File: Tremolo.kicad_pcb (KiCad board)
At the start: 2 copper layers, 177.9 x 90.1 mm, 116 parts, among them J1 Input, J10 R1, J11 R2, J12 TRG, J13 GND, J1A1 LeftA, J1B1 LeftB, J1C1 LeftC, J2 GND, J2A1 SwitchA, J2B1 SwitchB, J2C1 SwitchC, J3 +9v, J3A1 RightA, J3B1 RightB, J3C1 RightC, J4 GND, J5 RateSlv, J6 Gnd, J7 L2, J8 L1, J9 RateTip, Q1 BC549C, Q2 BC549C, Q3 BC549C, Q4 J113, Q5 BC549C, Q6 BC549C, T1 LeftTr, T2 RightTr, U1 TL072, U2 TL072, U3 TL072, U4 TL074, U5 VACTL, U6 VACTR

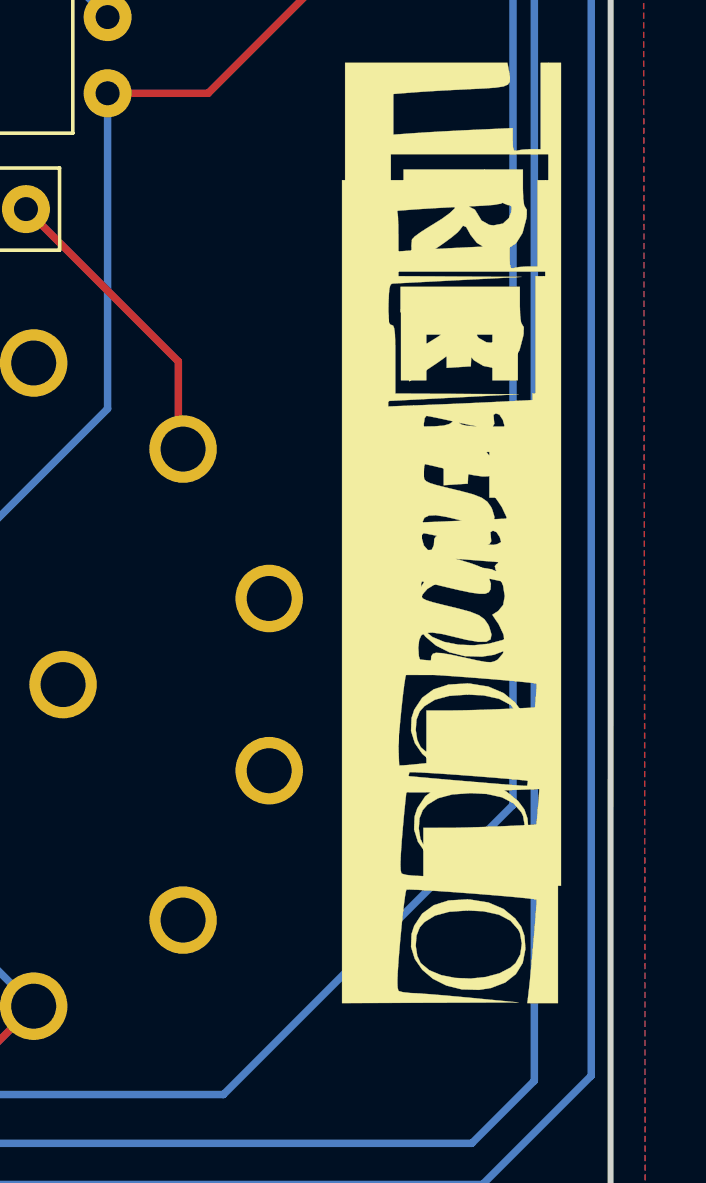
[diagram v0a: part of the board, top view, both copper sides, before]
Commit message: Removed extra logo footprints
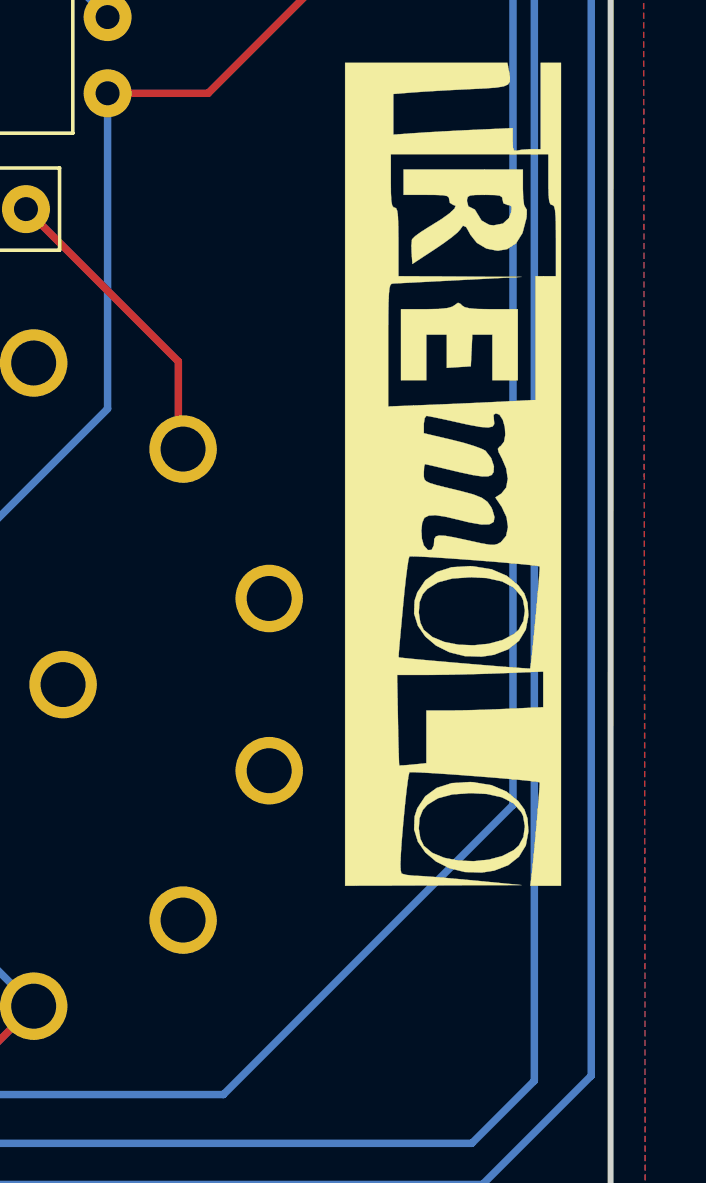
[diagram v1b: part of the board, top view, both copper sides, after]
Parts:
- removed the G*** at (81.9, 76.6)
- removed the G*** at (177.2, 97.7)
- removed the G*** at (219.2, 86.5)

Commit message: V2.0 provisionaly completed
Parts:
- removed D2, D3: LED, LED_THT:LED_D5.0mm
- removed J1A1: LeftA, Connector_Wire:SolderWire-0.25sqmm_1x03_P4.2mm_D0.65mm_OD1.7mm
- removed J1B1: LeftB, Connector_Wire:SolderWire-0.25sqmm_1x03_P4.2mm_D0.65mm_OD1.7mm
- removed J1C1: LeftC, Connector_Wire:SolderWire-0.25sqmm_1x03_P4.2mm_D0.65mm_OD1.7mm
- removed J2A1: SwitchA, Connector_Wire:SolderWire-0.25sqmm_1x03_P4.2mm_D0.65mm_OD1.7mm
- removed J2B1: SwitchB, Connector_Wire:SolderWire-0.25sqmm_1x03_P4.2mm_D0.65mm_OD1.7mm
- removed J2C1: SwitchC, Connector_Wire:SolderWire-0.25sqmm_1x03_P4.2mm_D0.65mm_OD1.7mm
- removed J3A1: RightA, Connector_Wire:SolderWire-0.25sqmm_1x03_P4.2mm_D0.65mm_OD1.7mm
- removed J3B1: RightB, Connector_Wire:SolderWire-0.25sqmm_1x03_P4.2mm_D0.65mm_OD1.7mm
- removed J3C1: RightC, Connector_Wire:SolderWire-0.25sqmm_1x03_P4.2mm_D0.65mm_OD1.7mm
- removed U5: VACTL, OptoDevice:PerkinElmer_VTL5C
- removed U6: VACTR, OptoDevice:PerkinElmer_VTL5C
- added DL3: LED, LED_THT:LED_D5.0mm, B.Cu at (135.3, 89.5)
- added DR2: LED, LED_THT:LED_D5.0mm, B.Cu at (125.1, 89.5)
- added J14: LSB1, Connector_Wire:SolderWire-0.25sqmm_1x01_D0.65mm_OD1.7mm, F.Cu at (192.0, 115.8)
- added J15: RSA1, Connector_Wire:SolderWire-0.25sqmm_1x01_D0.65mm_OD1.7mm, F.Cu at (65.5, 115.8)
- added J16: LSB2, Connector_Wire:SolderWire-0.25sqmm_1x01_D0.65mm_OD1.7mm, F.Cu at (195.2, 115.8)
- added J17: RSA2, Connector_Wire:SolderWire-0.25sqmm_1x01_D0.65mm_OD1.7mm, F.Cu at (68.8, 115.8)
- added J18: RSA3, Connector_Wire:SolderWire-0.25sqmm_1x01_D0.65mm_OD1.7mm, F.Cu at (72.0, 115.8)
- added J19: LSB3, Connector_Wire:SolderWire-0.25sqmm_1x01_D0.65mm_OD1.7mm, F.Cu at (198.5, 115.8)
- added J20: LSA1, Connector_Wire:SolderWire-0.25sqmm_1x01_D0.65mm_OD1.7mm, F.Cu at (182.2, 115.8)
- added J21: RSB1, Connector_Wire:SolderWire-0.25sqmm_1x01_D0.65mm_OD1.7mm, F.Cu at (75.3, 115.8)
- added J22: LSA3, Connector_Wire:SolderWire-0.25sqmm_1x01_D0.65mm_OD1.7mm, F.Cu at (188.7, 115.8)
- added J23: RSB3, Connector_Wire:SolderWire-0.25sqmm_1x01_D0.65mm_OD1.7mm, F.Cu at (81.8, 115.8)
- added J24: LSA2, Connector_Wire:SolderWire-0.25sqmm_1x01_D0.65mm_OD1.7mm, F.Cu at (185.5, 115.8)
- added J25: RSB2, Connector_Wire:SolderWire-0.25sqmm_1x01_D0.65mm_OD1.7mm, F.Cu at (78.5, 115.8)
- added J26: SWA1, Connector_Wire:SolderWire-0.25sqmm_1x01_D0.65mm_OD1.7mm, F.Cu at (124.1, 115.8)
- added J27: SWA2, Connector_Wire:SolderWire-0.25sqmm_1x01_D0.65mm_OD1.7mm, F.Cu at (127.4, 115.8)
- added J28: SWA3, Connector_Wire:SolderWire-0.25sqmm_1x01_D0.65mm_OD1.7mm, F.Cu at (130.6, 115.8)
- added J29: SWB1, Connector_Wire:SolderWire-0.25sqmm_1x01_D0.65mm_OD1.7mm, F.Cu at (133.9, 115.8)
- added J30: SWB2, Connector_Wire:SolderWire-0.25sqmm_1x01_D0.65mm_OD1.7mm, F.Cu at (137.1, 115.8)
- added J31: SWB3, Connector_Wire:SolderWire-0.25sqmm_1x01_D0.65mm_OD1.7mm, F.Cu at (140.4, 115.8)
- added VLD1: D_Photo, MyLibrary:LED_D5.0mm, F.Cu at (106.4, 90.8)
- added VLR1: D_LDR, MyLibrary:R_LDR_5.2x5.2mm_P3.5mm_Horizontal, F.Cu at (119.4, 100.8)
- added VRD1: D_Photo, MyLibrary:LED_D5.0mm, F.Cu at (106.4, 100.5)
- added VRR1: D_LDR, MyLibrary:R_LDR_5.2x5.2mm_P3.5mm_Horizontal, F.Cu at (119.4, 91.0)
- Q1, Q2, Q3, Q4, Q5, Q6: footprint Package_TO_SOT_THT:TO-92L_Inline_Wide -> MyLibrary:TO-92L_Inline_Wide
- moved C4 120.2 mm to (177.8, 73.2)
- moved C11 120.0 mm to (177.5, 66.8)
- moved R2 119.7 mm to (180.3, 71.9), turned to 0 degrees
- moved D4 117.4 mm to (190.8, 72.4), turned to 90 degrees
- moved R5 114.9 mm to (179.1, 76.7), turned to 0 degrees
- moved R13 109.7 mm to (180.3, 68.6), turned to 0 degrees
- moved R11 109.7 mm to (180.3, 65.3), turned to 0 degrees
- moved Q3 88.2 mm to (190.8, 80.3)
- moved G*** 84.8 mm to (134.5, 85.8), turned to 0 degrees
- moved J10 80.6 mm to (161.5, 41.3)
- moved J11 80.2 mm to (164.8, 41.3)
- moved C2 77.3 mm to (71.0, 66.6), turned to 0 degrees
- moved Q2 73.8 mm to (125.7, 111.8)
- moved C6 68.7 mm to (78.2, 66.8), turned to 0 degrees
- moved T1 65.5 mm to (111.7, 125.1)
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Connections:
- net /LB1 renamed Net-(C14-Pad2)
- net /RB1 renamed Net-(C15-Pad2)
- C7 pad 2: Net-(C5-Pad2) -> Net-(C7-Pad2)
- C8 pad 2: Net-(C5-Pad2) -> Net-(C7-Pad2)
- D4 pad 1: /RA1 -> Net-(D4-Pad1)
- D5 pad 1: /LA1 -> Net-(D5-Pad1)
- Q1 pad 3: Net-(Q1-Pad3) -> Net-(C5-Pad2)
- Q2 pad 1: /LA2 -> Net-(DL3-Pad1)
- Q3 pad 1: /RA2 -> Net-(DR2-Pad1)
- R8 pad 1: Net-(Q1-Pad3) -> Net-(C5-Pad2)
- R8 pad 2: Net-(C5-Pad2) -> Net-(C7-Pad2)
- RV1 pad 1: /LB2 -> Net-(C14-Pad1)
- RV1 pad 2: /LB2 -> Net-(RV1-Pad2)
- RV1 pad 3: Net-(C14-Pad1) -> Net-(RV1-Pad2)
- RV2 pad 1: /RB2 -> Net-(C15-Pad1)
- RV2 pad 2: /RB2 -> Net-(RV2-Pad2)
- RV2 pad 3: Net-(C15-Pad1) -> Net-(RV2-Pad2)
- RV3 pad 1: Net-(R32-Pad2) -> /Shape4
- RV3 pad 3: /Shape4 -> Net-(R32-Pad2)
- RV4 pad 1: Net-(R35-Pad2) -> /Shape12
- RV4 pad 3: /Shape12 -> Net-(R35-Pad2)
- U1 pad 5: GND -> VDC
- U3 pad 5: GND -> VDC
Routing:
- net VAA: track 146.9 -> 398.6 mm, vias 6 -> 0
- net GND: track 60.2 -> 291.2 mm, vias 6 -> 13
- net Net-(C1-Pad2): track 308.9 -> 121.0 mm, vias 2 -> 1
- net /MODEB: track 52.2 -> 216.4 mm, vias 0 -> 2
- net Net-(J17-Pad1): track 65.4 -> 214.4 mm, vias 0 -> 1
- net Net-(J7-Pad1): track 116.1 -> 260.6 mm
- net +9VA: track 58.4 -> 198.2 mm
- net Net-(J8-Pad1): track 123.2 -> 254.6 mm
- net Net-(D4-Pad1): track 0.00 -> 112.7 mm
- net /MODE4: track 163.1 -> 275.5 mm, vias 4 -> 5
- net /LA2: track 109.1 -> 0.00 mm, vias 3 -> 0
- net Net-(DR2-Pad1): track 0.00 -> 102.7 mm, vias 0 -> 1
- net Net-(C17-Pad2): track 20.1 -> 119.7 mm
- net Net-(C7-Pad2): track 0.00 -> 98.5 mm
- net Net-(C18-Pad2): track 26.2 -> 119.6 mm
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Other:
- board size 177.9 x 90.1 mm -> 138 x 100.9 mm
- net class Power added: clearance 0.5, trace_width 0.5, via_dia 0.8, via_drill 0.4
- net class Power2 added: clearance 0.3, trace_width 0.3, via_dia 0.8, via_drill 0.4
- board text added: "+9V"
- board text added: "A2"
- board text added: "A3"
- board text added: "B2"
- board text added: "B3"
- board text added: "BYPASS"
- board text added: "DC IN"
- board text added: "INPUT"
- board text added: "LDEPTH"
- board text added: "LEFT OUT"
- board text added: "LEFT SWITCH"
- board text added: "LFO-L-RATE"
- board text added: "LFO-R-RATE"
- board text added: "LTIP"
- board text added: "PEDAL"
- board text added: "RDEPTH"
- board text added: "RIGHT OUT"
- board text added: "RIGHT SWITCH"
- board text added: "RNG"
- board text added: "RTIP"
- board text added: "TRIGGER"
- board text added: "V2.0"
- board text removed: "9V"
- board text removed: "C1"
- board text removed: "L-Depth"
- board text removed: "L1"
- board text removed: "L2"
- board text removed: "LFO-L-Rate"
- board text removed: "LFO-R-Rate"
- board text removed: "R-Depth"
- board text removed: "R1"
- board text removed: "R2"
- board text removed: "V1.1"
